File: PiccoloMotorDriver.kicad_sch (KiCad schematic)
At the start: 0 parts

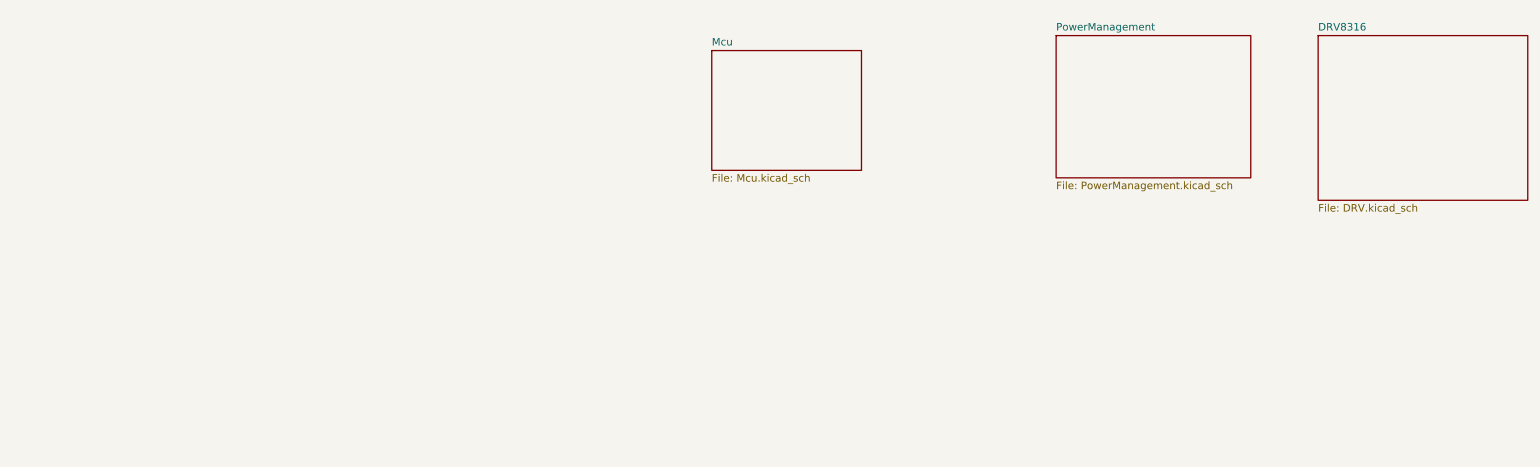
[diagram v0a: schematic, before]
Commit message: Add IO sub schematic, add communications
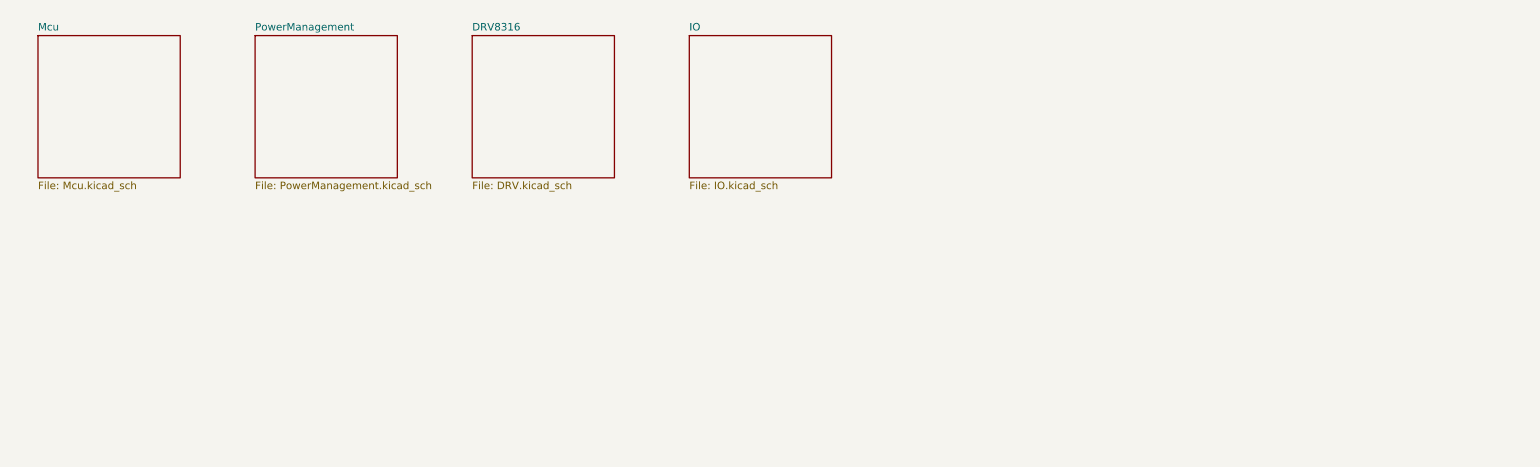
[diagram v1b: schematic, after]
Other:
- added sheet IO (IO.kicad_sch)

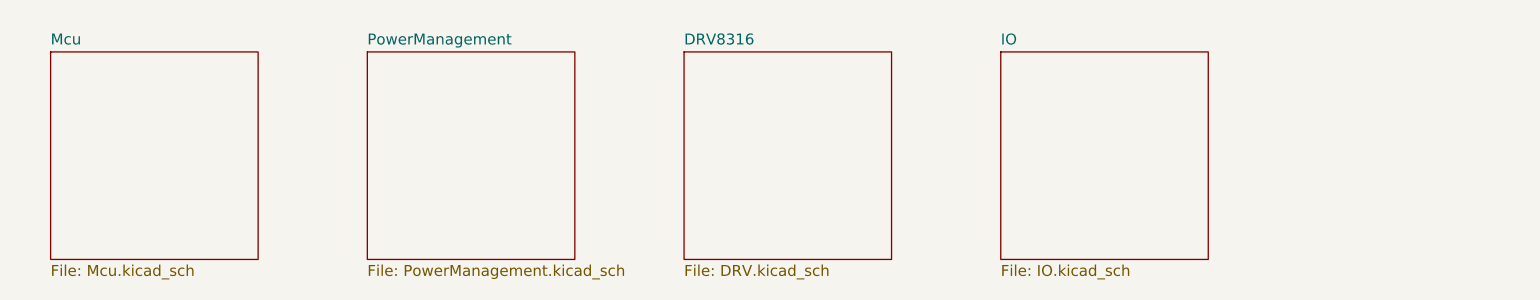
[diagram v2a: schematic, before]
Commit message: Add encoder sheet
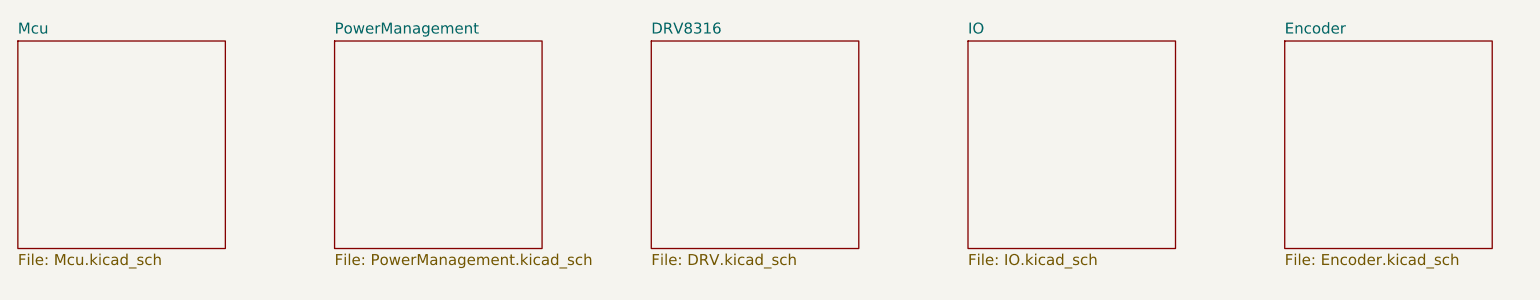
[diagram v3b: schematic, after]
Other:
- added sheet Encoder (Encoder.kicad_sch)
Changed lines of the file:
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@@
 	(paper "A5")
 	(sheet
-		(at 134.62 20.32)
+		(at 130.81 19.05)
 		(size 24.13 24.13)
 		(exclude_from_sim no)
@@
 		)
 		(property "Sheetname" "IO"
-			(at 134.62 19.6084 0)
+			(at 130.81 18.3384 0)
 			(effects
 				(font
@@
 		)
 		(property "Sheetfile" "IO.kicad_sch"
-			(at 134.62 45.0346 0)
+			(at 130.81 43.7646 0)
 			(effects
 				(font
@@
 	)
 	(sheet
-		(at 24.13 20.32)
+		(at 20.32 19.05)
 		(size 24.13 24.13)
 		(exclude_from_sim no)
@@
 		)
 		(property "Sheetname" "Mcu"
-			(at 24.13 19.6084 0)
+			(at 20.32 18.3384 0)
 			(effects
 				(font
@@
 		)
 		(property "Sheetfile" "Mcu.kicad_sch"
-			(at 24.13 45.0346 0)
+			(at 20.32 43.7646 0)
 			(effects
 				(font
@@
 	)
 	(sheet
-		(at 97.79 20.32)
+		(at 93.98 19.05)
 		(size 24.13 24.13)
 		(exclude_from_sim no)
@@
 		)
 		(property "Sheetname" "DRV8316"
-			(at 97.79 19.6084 0)
+			(at 93.98 18.3384 0)
 			(effects
 				(font
@@
 		)
 		(property "Sheetfile" "DRV.kicad_sch"
-			(at 97.79 45.0346 0)
+			(at 93.98 43.7646 0)
 			(effects
 				(font
@@
 	)
 	(sheet
-		(at 60.96 20.32)
+		(at 167.64 19.05)
+		(size 24.13 24.13)
+		(exclude_from_sim no)
+		(in_bom yes)
+		(on_board yes)
+		(dnp no)
+		(fields_autoplaced yes)
+		(stroke
+			(width 0.1524)
+			(type solid)
+		)
+		(fill
+			(color 203 0 255 1.0000)
+		)
+		(property "Sheetname" "Encoder"
+			(at 167.64 18.3384 0)
+			(effects
+				(font
+					(size 1.27 1.27)
+				)
+				(justify left bottom)
+			)
+		)
+		(property "Sheetfile" "Encoder.kicad_sch"
+			(at 167.64 43.7646 0)
+			(effects
+				(font
+					(size 1.27 1.27)
+				)
+				(justify left top)
+			)
+		)
+		(instances
+			(project "PiccoloMotorDriver"
+				(path "/cc8a13e7-b1a6-4cbd-adcd-4feb8b2e2369"
+					(page "7")
+				)
+			)
+		)
+	)
+	(sheet
+		(at 57.15 19.05)
 		(size 24.13 24.13)
 		(exclude_from_sim no)
@@
 		)
 		(property "Sheetname" "PowerManagement"
-			(at 60.96 19.6084 0)
+			(at 57.15 18.3384 0)
 			(effects
 				(font
@@
 		)
 		(property "Sheetfile" "PowerManagement.kicad_sch"
-			(at 60.96 45.0346 0)
+			(at 57.15 43.7646 0)
 			(effects
 				(font

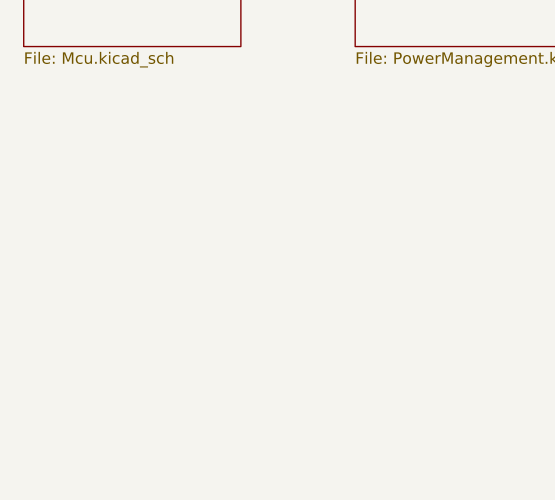
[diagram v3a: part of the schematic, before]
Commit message: Added DRV layout
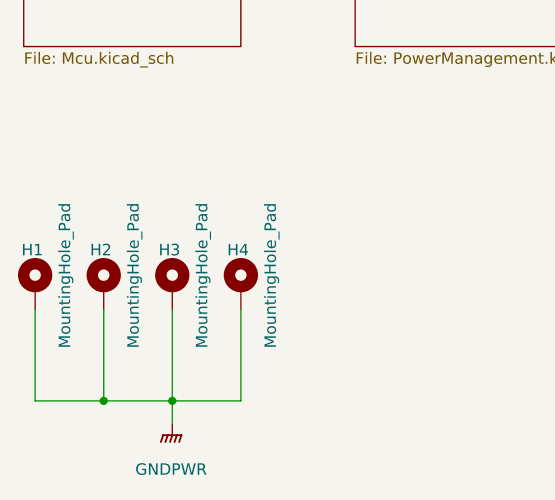
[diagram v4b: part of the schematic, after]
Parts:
- added H1, H2, H3, H4: MountingHole_Pad, MountingHole:MountingHole_3.2mm_M3_Pad_Via, symbol Mechanical:MountingHole_Pad
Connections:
- new net GNDPWR: H1.1, H2.1, H3.1, H4.1

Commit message: more layout
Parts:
- added FID1, FID2, FID3: Fiducial, Fiducial:Fiducial_0.5mm_Mask1mm, symbol Mechanical:Fiducial
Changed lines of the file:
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@@
+	)
+	(symbol
+		(lib_id "Mechanical:Fiducial")
+		(at 85.09 68.58 0)
+		(unit 1)
+		(exclude_from_sim no)
+		(in_bom no)
+		(on_board yes)
+		(dnp no)
+		(fields_autoplaced yes)
+		(property "Reference" "FID3"
+			(at 87.63 67.3099 0)
+			(effects
+				(font
+					(size 1.27 1.27)
+				)
+				(justify left)
+			)
+		)
+		(property "Value" "Fiducial"
+			(at 87.63 69.8499 0)
+			(effects
+				(font
+					(size 1.27 1.27)
+				)
+				(justify left)
+			)
+		)
+		(property "Footprint" "Fiducial:Fiducial_0.5mm_Mask1mm"
+			(at 85.09 68.58 0)
+			(effects
+				(font
+					(size 1.27 1.27)
+				)
+				(hide yes)
+			)
+		)
+		(property "Datasheet" "~"
+			(at 85.09 68.58 0)
+			(effects
+				(font
+					(size 1.27 1.27)
+				)
+				(hide yes)
+			)
+		)
+		(property "Description" "Fiducial Marker"
+			(at 85.09 68.58 0)
+			(effects
+				(font
+					(size 1.27 1.27)
+				)
+				(hide yes)
+			)
+		)
+		(instances
+			(project ""
+				(path "/cc8a13e7-b1a6-4cbd-adcd-4feb8b2e2369"
+					(reference "FID3")
+					(unit 1)
+				)
+			)
+		)
 	)
 	(symbol
@@
 	)
 	(symbol
+		(lib_id "Mechanical:Fiducial")
+		(at 72.39 68.58 0)
+		(unit 1)
+		(exclude_from_sim no)
+		(in_bom no)
+		(on_board yes)
+		(dnp no)
+		(fields_autoplaced yes)
+		(property "Reference" "FID2"
+			(at 74.93 67.3099 0)
+			(effects
+				(font
+					(size 1.27 1.27)
+				)
+				(justify left)
+			)
+		)
+		(property "Value" "Fiducial"
+			(at 74.93 69.8499 0)
+			(effects
+				(font
+					(size 1.27 1.27)
+				)
+				(justify left)
+			)
+		)
+		(property "Footprint" "Fiducial:Fiducial_0.5mm_Mask1mm"
+			(at 72.39 68.58 0)
+			(effects
+				(font
+					(size 1.27 1.27)
+				)
+				(hide yes)
+			)
+		)
+		(property "Datasheet" "~"
+			(at 72.39 68.58 0)
+			(effects
+				(font
+					(size 1.27 1.27)
+				)
+				(hide yes)
+			)
+		)
+		(property "Description" "Fiducial Marker"
+			(at 72.39 68.58 0)
+			(effects
+				(font
+					(size 1.27 1.27)
+				)
+				(hide yes)
+			)
+		)
+		(instances
+			(project ""
+				(path "/cc8a13e7-b1a6-4cbd-adcd-4feb8b2e2369"
+					(reference "FID2")
+					(unit 1)
+				)
+			)
+		)
+	)
+	(symbol
 		(lib_id "Mechanical:MountingHole_Pad")
 		(at 21.59 69.85 0)
@@
 					(unit 1)
 				)
+			)
+		)
+	)
+	(symbol
+		(lib_id "Mechanical:Fiducial")
+		(at 59.69 68.58 0)
+		(unit 1)
+		(exclude_from_sim no)
+		(in_bom no)
+		(on_board yes)
+		(dnp no)
+		(fields_autoplaced yes)
+		(property "Reference" "FID1"
+			(at 62.23 67.3099 0)
+			(effects
+				(font
+					(size 1.27 1.27)
+				)
+				(justify left)
+			)
+		)
+		(property "Value" "Fiducial"
+			(at 62.23 69.8499 0)
+			(effects
+				(font
+					(size 1.27 1.27)
+				)
+				(justify left)
+			)
+		)
+		(property "Footprint" "Fiducial:Fiducial_0.5mm_Mask1mm"
+			(at 59.69 68.58 0)
+			(effects
+				(font
+					(size 1.27 1.27)
+				)
+				(hide yes)
+			)
+		)
+		(property "Datasheet" "~"
+			(at 59.69 68.58 0)
+			(effects
+				(font
+					(size 1.27 1.27)
+				)
+				(hide yes)
+			)
+		)
+		(property "Description" "Fiducial Marker"
+			(at 59.69 68.58 0)
+			(effects
+				(font
+					(size 1.27 1.27)
+				)
+				(hide yes)
+			)
+		)
+		(instances
+			(project ""
+				(path "/cc8a13e7-b1a6-4cbd-adcd-4feb8b2e2369"
+					(reference "FID1")
+					(unit 1)
+				)
